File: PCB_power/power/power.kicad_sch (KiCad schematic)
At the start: 33 parts, among them J3 S2B-PH-SM4-TB, Q4 DMG3415UQ-7, SW1 SLW-121586-5A-D, U4 LM66100DCK, U6 BQ21040DBV, U7 TLV75733PDBV, U8 TLV61048, U9 MCP1825ST-5002E/DB

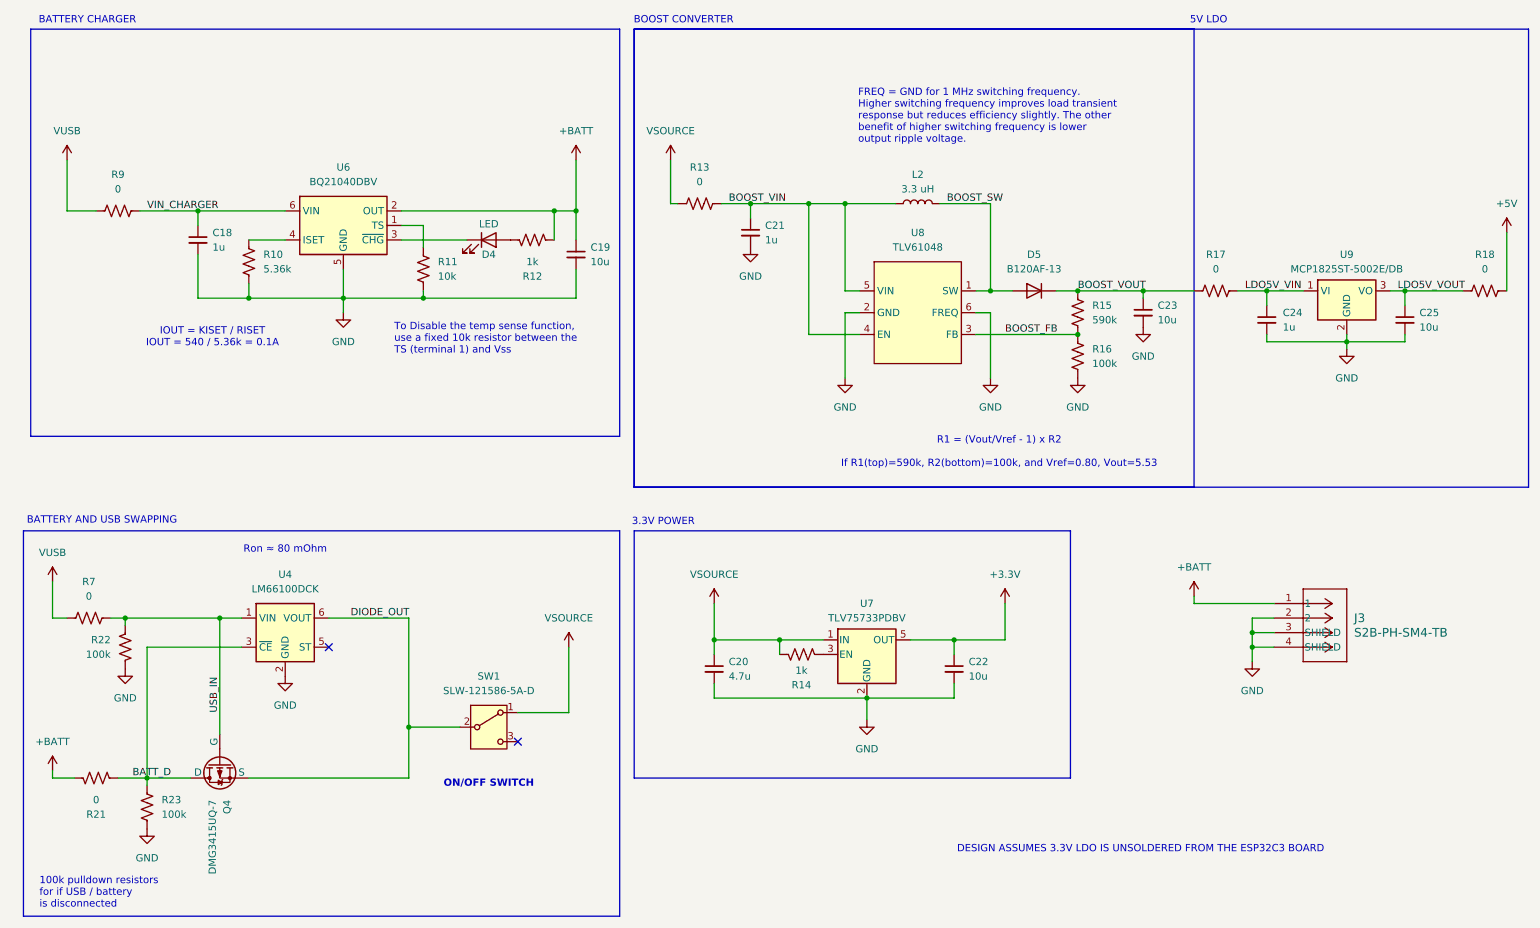
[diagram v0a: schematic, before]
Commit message: power - added headers, decoupling cap, changed inductor, 3d models
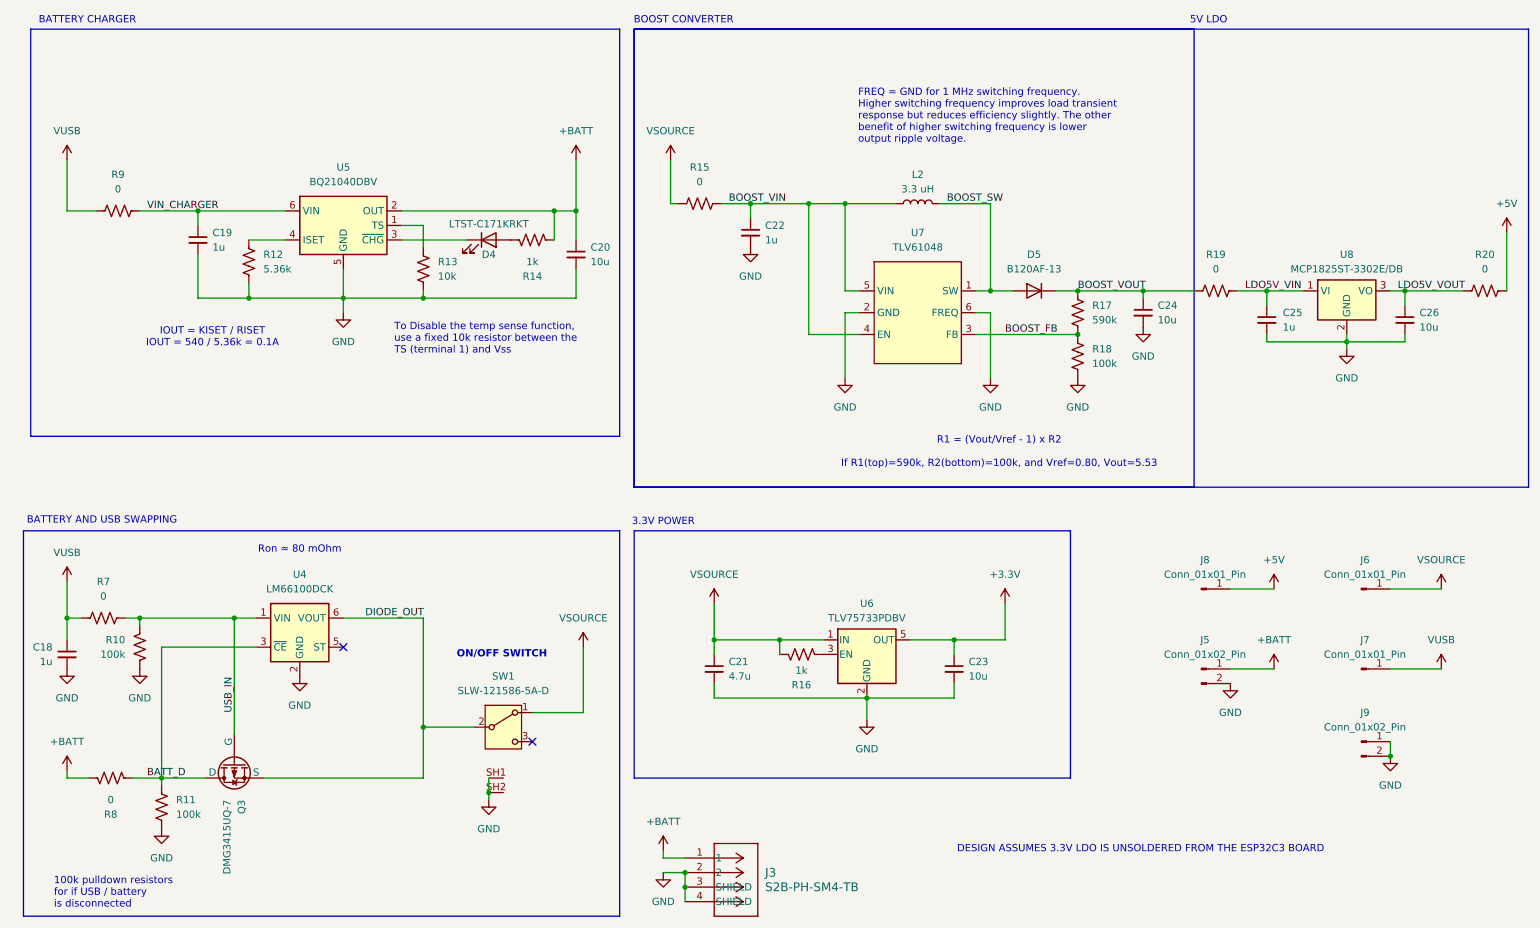
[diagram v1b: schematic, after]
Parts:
- added C18: 1u, Capacitor_SMD:C_0805_2012Metric_Pad1.18x1.45mm_HandSolder, symbol Device:C_Small
- added J5, J9: Conn_01x02_Pin, Connector_PinHeader_2.54mm:PinHeader_1x02_P2.54mm_Vertical, symbol Connector:Conn_01x02_Pin
- added J6, J7, J8: Conn_01x01_Pin, Connector_PinHeader_2.54mm:PinHeader_1x01_P2.54mm_Vertical, symbol Connector:Conn_01x01_Pin
- D4: value LED -> LTST-C171KRKT
- L2: footprint Library:IND_VLS6045AF-3R3N -> Library:IND_SWPA5040S_SNL
- U8: renamed from U9; value MCP1825ST-5002E/DB -> MCP1825ST-3302E/DB
- renumbered C18 to C19, C19 to C20, C20 to C21, C21 to C22, C22 to C23, C23 to C24, C24 to C25, C25 to C26, Q4 to Q3, R22 to R10, R23 to R11, R10 to R12, R11 to R13, R12 to R14, R13 to R15, R14 to R16, R15 to R17, R16 to R18, R17 to R19, R18 to R20, R21 to R8, U6 to U5, U7 to U6, U8 to U7
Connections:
- net +5V: now also J8.1 (Pin_1)
- net +BATT: now also J5.1 (Pin_1)
- net GND: now also SW1.SH1, SW1.SH2, C18.2, J5.2 (Pin_2), J9.1 (Pin_1), J9.2 (Pin_2)
- net VSOURCE: now also J6.1 (Pin_1)
- net VUSB: now also C18.1, J7.1 (Pin_1)
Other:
- moved on the sheet: Q3, R10, R11, R7, R8, U4

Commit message: annotate
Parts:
- renumbered J8 to J4, J9 to J8

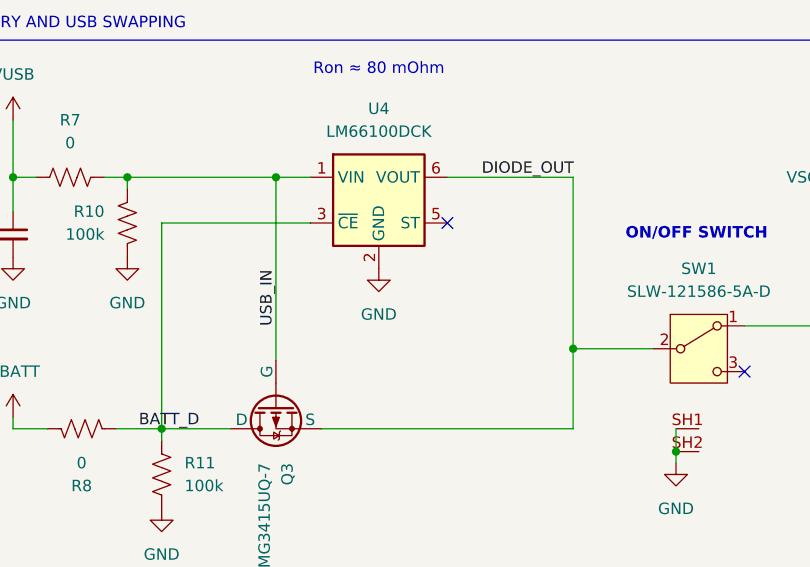
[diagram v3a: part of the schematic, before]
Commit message: changed inductor. did some SPICE sims
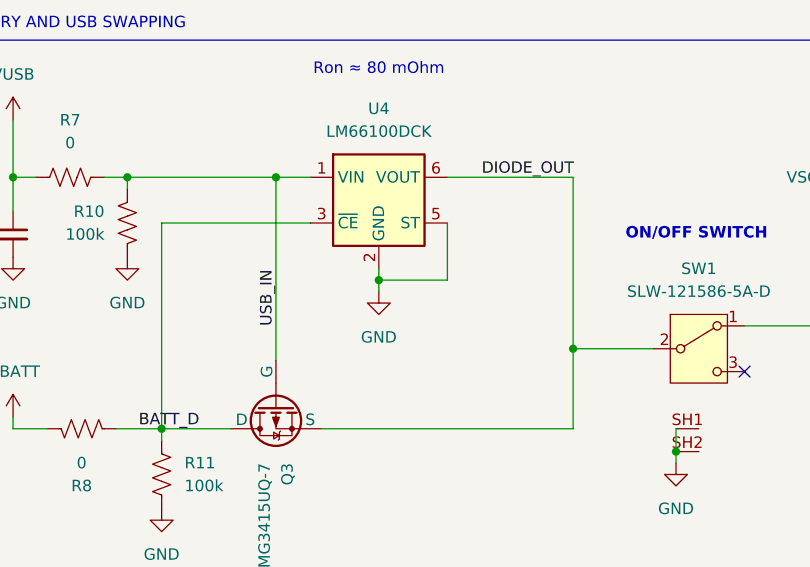
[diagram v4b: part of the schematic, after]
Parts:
- L2: footprint Library:IND_SWPA5040S_SNL -> Library:IND_VLS6045AF-3R3N
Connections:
- net GND: now also U4.5 (ST)
- no-connect marks 2 -> 1
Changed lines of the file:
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@@
 	)
 	(junction
+		(at 64.77 140.97)
+		(diameter 0)
+		(color 0 0 0 0)
+	)
+	(junction
 		(at 257.81 72.39)
 		(diameter 0)
@@
 	)
 	(no_connect
-		(at 72.39 134.62)
-	)
-	(no_connect
 		(at 105.41 151.13)
 	)
@@
 	(wire
 		(pts
+			(xy 72.39 140.97) (xy 64.77 140.97)
+		)
+		(stroke
+			(width 0)
+			(type default)
+		)
+	)
+	(wire
+		(pts
 			(xy 185.42 76.2) (xy 185.42 87.63)
 		)
@@
 	(wire
 		(pts
+			(xy 64.77 142.24) (xy 64.77 140.97)
+		)
+		(stroke
+			(width 0)
+			(type default)
+		)
+	)
+	(wire
+		(pts
 			(xy 34.29 129.54) (xy 36.83 129.54)
 		)
@@
 	(wire
 		(pts
+			(xy 64.77 140.97) (xy 64.77 139.7)
+		)
+		(stroke
+			(width 0)
+			(type default)
+		)
+	)
+	(wire
+		(pts
 			(xy 247.65 81.28) (xy 247.65 82.55)
 		)
@@
 	(wire
 		(pts
+			(xy 72.39 134.62) (xy 72.39 140.97)
+		)
+		(stroke
+			(width 0)
+			(type default)
+		)
+	)
+	(wire
+		(pts
 			(xy 137.16 127) (xy 137.16 133.35)
 		)
@@
 			)
 		)
-		(property "Footprint" "Library:IND_SWPA5040S_SNL"
+		(property "Footprint" "Library:IND_VLS6045AF-3R3N"
 			(at 172.72 57.15 0)
 			(effects
@@
 			)
 		)
-		(property "Datasheet" "~"
+		(property "Datasheet" "https://www.digikey.com/en/products/detail/tdk-corporation/VLS6045AF-3R3N/9596880"
 			(at 172.72 57.15 0)
 			(effects
@@
 			)
 		)
-		(property "Description" "Inductor"
+		(property "Description" "VLS6045AF-3R3N"
 			(at 172.72 57.15 0)
 			(effects
@@
 	(symbol
 		(lib_id "power:GND")
-		(at 64.77 139.7 0)
+		(at 64.77 142.24 0)
 		(unit 1)
 		(exclude_from_sim no)
@@
 		(dnp no)
 		(property "Reference" "#PWR022"
-			(at 64.77 146.05 0)
+			(at 64.77 148.59 0)
 			(effects
 				(font
@@
 		)
 		(property "Value" "GND"
-			(at 64.77 144.78 0)
+			(at 64.77 147.32 0)
 			(effects
 				(font
@@
 		)
 		(property "Footprint" ""
-			(at 64.77 139.7 0)
+			(at 64.77 142.24 0)
 			(effects
 				(font
@@
 		)
 		(property "Datasheet" ""
-			(at 64.77 139.7 0)
+			(at 64.77 142.24 0)
 			(effects
 				(font
@@
 		)
 		(property "Description" "Power symbol creates a global label with name \"GND\" , ground"
-			(at 64.77 139.7 0)
+			(at 64.77 142.24 0)
 			(effects
 				(font

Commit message: MCB
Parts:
- L2: value 3.3 uH -> 3.3uH
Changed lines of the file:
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@@
 			)
 		)
-		(property "Value" "3.3 uH"
+		(property "Value" "3.3uH"
 			(at 172.72 54.61 90)
 			(effects

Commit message: added power digikey links
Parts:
- removed J3: S2B-PH-SM4-TB, Library:CONN_S2B-PH-SM4-TB_JST, symbol SymbolLibrary:S2B-PH-SM4-TB
- added J3: S2B-PH-K-SLFSN, Library:CONN_S2B-PH-K-S_JST, symbol SymbolLibrary:S2B-PH-K-SLFSN
- C18, C19, C22, C25: Part Number (none) -> CL21B105KBFNNNE
- C20, C23, C24, C26: Part Number (none) -> GRM21BR61H106KE43L
- C21: Part Number (none) -> GRM21BR61H475KE51L
- R10, R11, R18: Part Number (none) -> AC0805FR-07100KL
- R12: Part Number (none) -> ERA-6AEB5361V
- R13: Part Number (none) -> RC0805FR-0710KL
- R14, R16: Part Number (none) -> AC0805FR-071KL
- R15, R19, R20, R7, R8, R9: Part Number (none) -> RC0805JR-070RL
- R17: Part Number (none) -> RC0805FR-07590KL
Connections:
- net +BATT: now also J3.1
- net GND: now also J3.2

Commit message: pushing all updates
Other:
- note removed: "IOUT = KISET / RISET IOUT = 540 / 5.36k = 0.1A"
- note removed: "To Disable the temp sense function, use a fixed 10k resistor between the TS (terminal 1) and Vss"
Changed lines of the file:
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@@
-		)
-	)
-	(text "To Disable the temp sense function, \nuse a fixed 10k resistor between the \nTS (terminal 1) and Vss"
-		(exclude_from_sim no)
-		(at 81.28 80.772 0)
-		(effects
-			(font
-				(size 1.27 1.27)
-			)
-			(justify left)
 		)
 	)
@@
 		(effects
 			(font
-				(size 1.27 1.27)
-			)
-		)
-	)
-	(text "IOUT = KISET / RISET\nIOUT = 540 / 5.36k = 0.1A\n"
-		(exclude_from_sim no)
-		(at 49.53 80.518 0)
-		(effects
-			(font
